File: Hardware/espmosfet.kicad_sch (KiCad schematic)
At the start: 48 parts, among them J1 USB_B_Micro, J2 Conn_01x04_Male, J3 USB_A, J4 Conn_01x04_Male, J5 Conn_01x02_Male, J6 Conn_01x02_Male, J7 Conn_01x03_Male, Q1 AO3400A, Q2 AO3400A, U1 TPS2514A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

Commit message: fix
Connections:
- net +5V: now also U1.5 (IN)
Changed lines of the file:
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@@
+    (stroke (width 0) (type default) (color 0 0 0 0))
+  )
+  (wire (pts (xy 246.38 41.91) (xy 250.19 41.91))
     (stroke (width 0) (type default) (color 0 0 0 0))
   )
@@
     (stroke (width 0) (type default) (color 0 0 0 0))
   )
-  (wire (pts (xy 246.38 41.91) (xy 265.43 41.91))
-    (stroke (width 0) (type default) (color 0 0 0 0))
-  )
   (wire (pts (xy 199.39 144.78) (xy 199.39 147.32))
     (stroke (width 0) (type default) (color 0 0 0 0))
@@
     (stroke (width 0) (type default) (color 0 0 0 0))
   )
-  (wire (pts (xy 250.19 33.02) (xy 250.19 31.75))
-    (stroke (width 0) (type default) (color 0 0 0 0))
-  )
   (wire (pts (xy 116.84 30.48) (xy 110.49 30.48))
     (stroke (width 0) (type default) (color 0 0 0 0))
@@
   )
   (wire (pts (xy 176.53 68.58) (xy 184.15 68.58))
-    (stroke (width 0) (type default) (color 0 0 0 0))
-  )
-  (wire (pts (xy 265.43 41.91) (xy 265.43 26.67))
     (stroke (width 0) (type default) (color 0 0 0 0))
   )
@@
     (pin "5")
   )
-  (symbol (lib_id "power:GND") (at 250.19 33.02 0) (unit 1)
-    (in_bom yes) (on_board yes)
-    (property "Reference" "#PWR03" (id 0) (at 250.19 39.37 0)
-      (effects (font (size 1.27 1.27)) hide)
-    )
-    (property "Value" "GND" (id 1) (at 250.317 37.4142 0))
-    (property "Footprint" "" (id 2) (at 250.19 33.02 0)
-      (effects (font (size 1.27 1.27)) hide)
-    )
-    (property "Datasheet" "" (id 3) (at 250.19 33.02 0)
+  (symbol (lib_id "power:GND") (at 250.19 31.75 90) (unit 1)
+    (in_bom yes) (on_board yes)
+    (property "Reference" "#PWR03" (id 0) (at 256.54 31.75 0)
+      (effects (font (size 1.27 1.27)) hide)
+    )
+    (property "Value" "GND" (id 1) (at 254.5842 31.623 0))
+    (property "Footprint" "" (id 2) (at 250.19 31.75 0)
+      (effects (font (size 1.27 1.27)) hide)
+    )
+    (property "Datasheet" "" (id 3) (at 250.19 31.75 0)
       (effects (font (size 1.27 1.27)) hide)
     )
@@
     )
     (property "Datasheet" "" (id 3) (at 60.96 110.49 0)
+      (effects (font (size 1.27 1.27)) hide)
+    )
+    (pin "1")
+  )
+  (symbol (lib_id "power:+5V") (at 250.19 41.91 270) (unit 1)
+    (in_bom yes) (on_board yes)
+    (property "Reference" "#PWR0124" (id 0) (at 246.38 41.91 0)
+      (effects (font (size 1.27 1.27)) hide)
+    )
+    (property "Value" "+5V" (id 1) (at 254.5842 42.291 0))
+    (property "Footprint" "" (id 2) (at 250.19 41.91 0)
+      (effects (font (size 1.27 1.27)) hide)
+    )
+    (property "Datasheet" "" (id 3) (at 250.19 41.91 0)
       (effects (font (size 1.27 1.27)) hide)
     )
@@
       (reference "#PWR0123") (unit 1) (value "+5V") (footprint "")
     )
+    (path "/0932daf5-053b-464b-bc20-4d6ccf3ec231"
+      (reference "#PWR0124") (unit 1) (value "+5V") (footprint "")
+    )
     (path "/00000000-0000-0000-0000-000061bdbf9c"

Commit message: add USB-C input
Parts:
- added P1: USB_C_Receptacle_USB2.0, Connector_USB:USB_C_Receptacle_XKB_U262-16XN-4BVC11, symbol Connector:USB_C_Receptacle_USB2.0
- added R18: 1M, Resistor_SMD:R_0805_2012Metric, symbol Device:R
- added R19, R20: 5.11k, Resistor_SMD:R_0805_2012Metric, symbol Device:R
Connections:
- net +5VD: now also P1.A4 (VBUS), P1.A9 (VBUS), P1.B4 (VBUS), P1.B9 (VBUS)
- net GND: now also P1.A1 (GND), P1.A12 (GND), P1.B1 (GND), P1.B12 (GND), R18.1, R19.2, R20.2
- new net: P1.A5 (CC1), R20.1
- new net: P1.A6 (D+), P1.B6 (D+)
- new net: P1.A7 (D-), P1.B7 (D-)
- new net: P1.B5 (CC2), R19.1
- new net: P1.S1 (SHIELD), R18.2

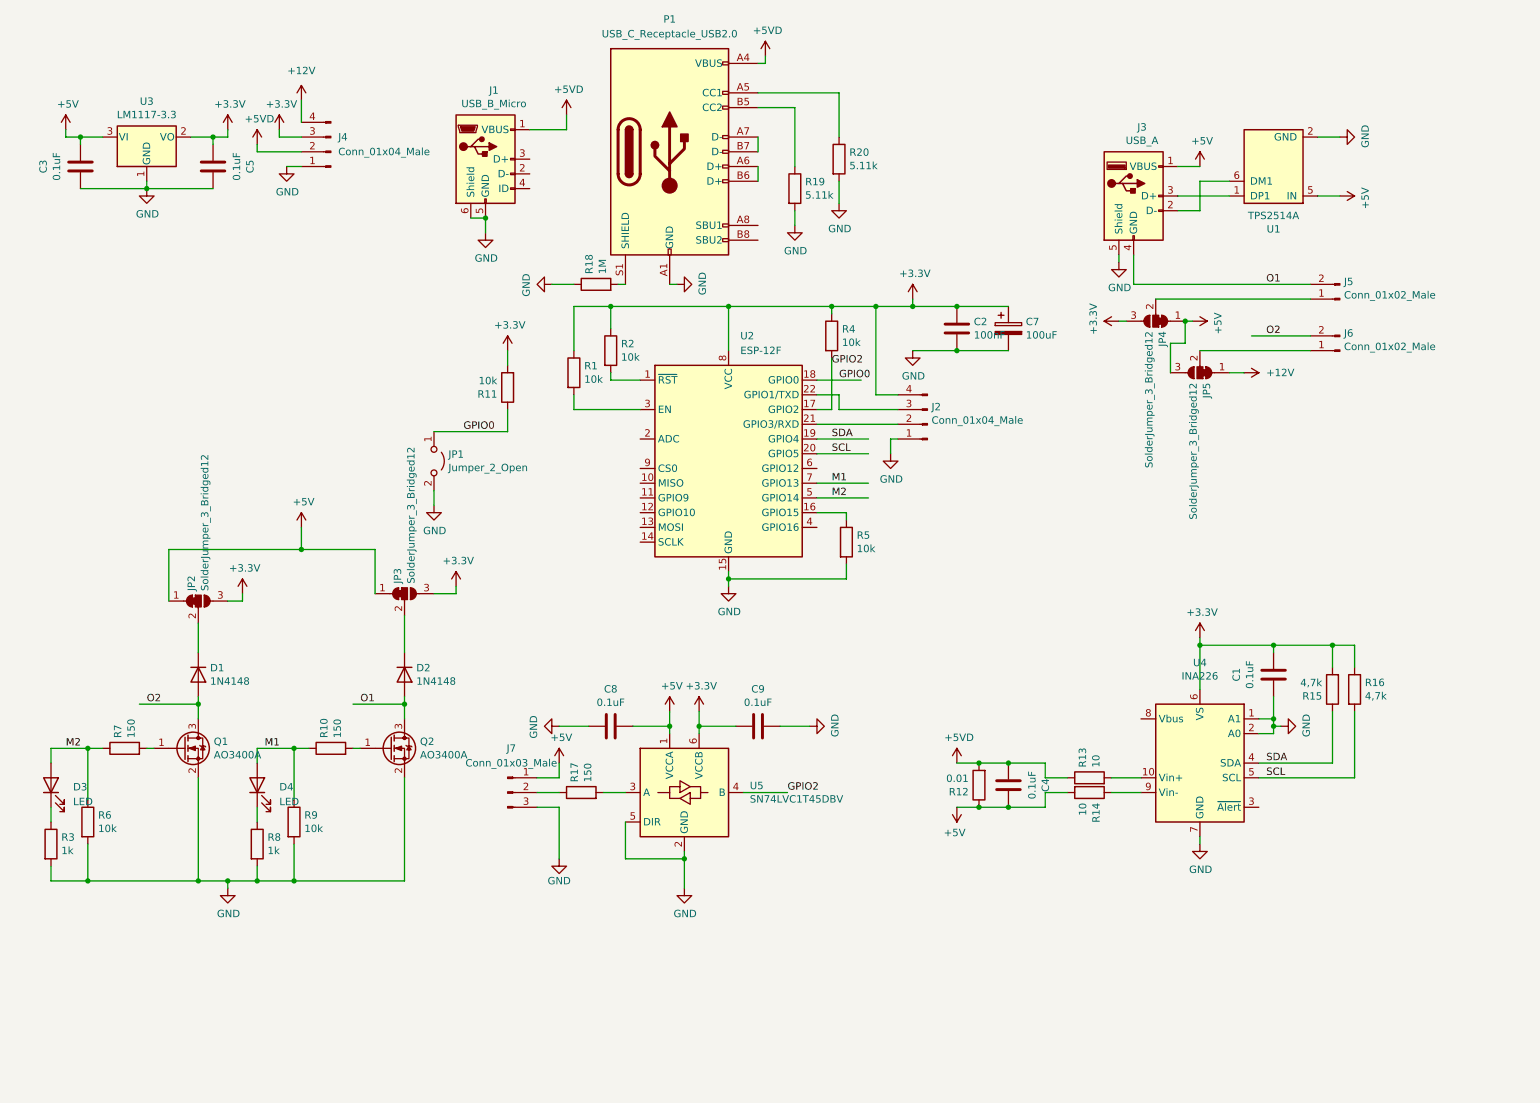
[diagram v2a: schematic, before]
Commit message: add ws2812b on board, add USB-C Output
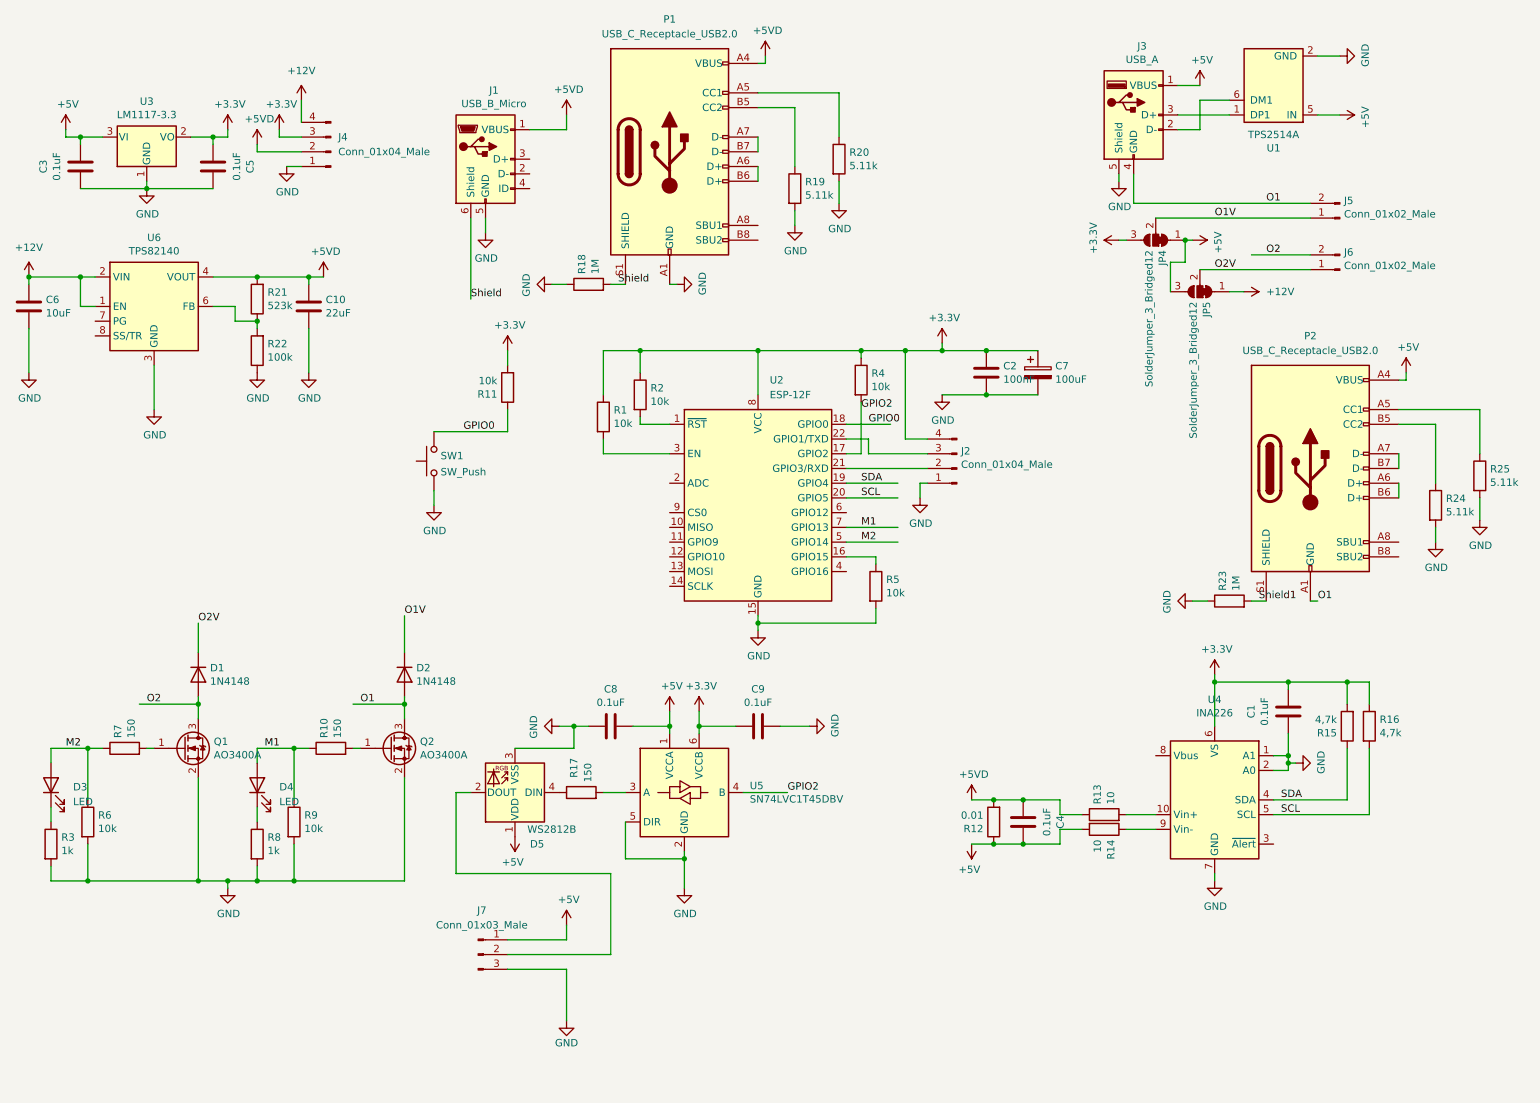
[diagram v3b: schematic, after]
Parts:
- removed JP1: Jumper_2_Open, Jumper:SolderJumper-2_P1.3mm_Open_Pad1.0x1.5mm, symbol Jumper:Jumper_2_Open
- removed JP2, JP3: SolderJumper_3_Bridged12, Jumper:SolderJumper-3_P1.3mm_Bridged12_Pad1.0x1.5mm, symbol Jumper:SolderJumper_3_Bridged12
- added C10: 22uF, Capacitor_SMD:C_1206_3216Metric, symbol Device:C
- added C6: 10uF, Capacitor_SMD:C_0603_1608Metric, symbol Device:C
- added D5: WS2812B, LED_SMD:LED_WS2812B_PLCC4_5.0x5.0mm_P3.2mm, symbol LED:WS2812B
- added P2: USB_C_Receptacle_USB2.0, Connector_USB:USB_C_Receptacle_XKB_U262-16XN-4BVC11, symbol Connector:USB_C_Receptacle_USB2.0
- added R21: 523k, Resistor_SMD:R_0805_2012Metric, symbol Device:R
- added R22: 100k, Resistor_SMD:R_0805_2012Metric, symbol Device:R
- added R23: 1M, Resistor_SMD:R_0805_2012Metric, symbol Device:R
- added R24, R25: 5.11k, Resistor_SMD:R_0805_2012Metric, symbol Device:R
- added SW1: SW_Push, Button_Switch_SMD:SW_Push_SPST_NO_Alps_SKRK, symbol Switch:SW_Push
- added U6: TPS82140, Package_LGA:Texas_SIL0008D_MicroSiP-8-1EP_2.8x3mm_P0.65mm_EP1.1x1.9mm_ThermalVias, symbol Regulator_Switching:TPS82140
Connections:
- net +12V: now also C6.1, U6.1 (EN), U6.2 (VIN)
- net +5V: now also D5.1 (VDD), P2.A4 (VBUS), P2.A9 (VBUS), P2.B4 (VBUS), P2.B9 (VBUS)
- net +5VD: now also C10.1, R21.2, U6.4 (VOUT), U6.5 (VOUT)
- net GND: now also C10.2, C6.2, D5.3 (VSS), R22.1, R23.1, R24.2, R25.2, SW1.1, U6.3 (GND), U6.9 (GND); no longer J1.6 (Shield)
- net GPIO0: now also SW1.2
- net O1: now also P2.A1 (GND), P2.A12 (GND), P2.B1 (GND), P2.B12 (GND)
- net O1V: now reaches D2.1 (K)
- net O1V: now also J5.1 (Pin_1), JP4.2 (C)
- net O2V: now reaches D1.1 (K)
- net O2V: now also J6.1 (Pin_1), JP5.2 (C)
- net at J7.2 (Pin_2): now also D5.2 (DOUT); no longer R17.1
- net Shield: now reaches P1.S1 (SHIELD), R18.2
- net Shield: now also J1.6 (Shield)
- new net: D5.4 (DIN), R17.1
- new net: P2.B5 (CC2), R24.1
- new net: R21.1, R22.2, U6.6 (FB)
- new net: P2.A5 (CC1), R25.1
- new net: P2.A6 (D+), P2.B6 (D+)
- new net: P2.A7 (D-), P2.B7 (D-)
- new net Shield1: P2.S1 (SHIELD), R23.2
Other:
- moved on the sheet: C1, C2, C4, C7, J2, J3, J5, J6, J7, JP4, JP5, R1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

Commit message: update to V2 Version
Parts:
- removed R21: 523k, Resistor_SMD:R_0805_2012Metric, symbol Device:R
- removed R22: 100k, Resistor_SMD:R_0805_2012Metric, symbol Device:R
- removed U6: TPS82140, Package_LGA:Texas_SIL0008D_MicroSiP-8-1EP_2.8x3mm_P0.65mm_EP1.1x1.9mm_ThermalVias, symbol Regulator_Switching:TPS82140
- added U6: LMZM23601V5, Package_LGA:Texas_SIL0010A_MicroSiP-10-1EP_3.8x3mm_P0.6mm_EP0.7x2.9mm_ThermalVias, symbol Regulator_Switching:LMZM23601V5
- C10: footprint Capacitor_SMD:C_1206_3216Metric -> Capacitor_SMD:C_0805_2012Metric
- R19, R20, R24, R25: footprint Resistor_SMD:R_0805_2012Metric -> Resistor_SMD:R_0603_1608Metric
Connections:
- net +12V: now also U6.3 (VIN), U6.4 (EN)
- net +5VD: now also U6.6 (VOUT), U6.7 (FB)
- net GND: now also U6.1 (GND), U6.11 (GND), U6.2 (MODE/SYNC)
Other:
- moved on the sheet: C10, C6

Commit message: adjust Readme
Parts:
- added JP1: Jumper_2_Open, Jumper:SolderJumper-2_P1.3mm_Open_Pad1.0x1.5mm, symbol Jumper:Jumper_2_Open
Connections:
- net at D5.2 (DOUT), J7.2 (Pin_2): now also JP1.1 (A)
- net at D5.4 (DIN), R17.1: now also JP1.2 (B)
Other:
- moved on the sheet: R17
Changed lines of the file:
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@@
   (junction (at 31.75 73.66) (diameter 0) (color 0 0 0 0)
   )
+  (junction (at 124.46 158.75) (diameter 0) (color 0 0 0 0)
+  )
   (junction (at 195.58 146.05) (diameter 0) (color 0 0 0 0)
   )
@@
   (junction (at 27.94 88.9) (diameter 0) (color 0 0 0 0)
   )
+  (junction (at 115.57 144.78) (diameter 0) (color 0 0 0 0)
+  )
   (junction (at 181.61 68.58) (diameter 0) (color 0 0 0 0)
   )
@@
     (stroke (width 0) (type default) (color 0 0 0 0))
   )
+  (wire (pts (xy 115.57 148.59) (xy 115.57 144.78))
+    (stroke (width 0) (type default) (color 0 0 0 0))
+  )
   (wire (pts (xy 44.45 40.64) (xy 55.88 40.64))
     (stroke (width 0) (type default) (color 0 0 0 0))
@@
     (stroke (width 0) (type default) (color 0 0 0 0))
   )
-  (wire (pts (xy 123.19 144.78) (xy 127 144.78))
-    (stroke (width 0) (type default) (color 0 0 0 0))
-  )
   (wire (pts (xy 27.94 157.48) (xy 27.94 160.02))
     (stroke (width 0) (type default) (color 0 0 0 0))
@@
     (stroke (width 0) (type default) (color 0 0 0 0))
   )
+  (wire (pts (xy 124.46 144.78) (xy 127 144.78))
+    (stroke (width 0) (type default) (color 0 0 0 0))
+  )
   (wire (pts (xy 88.9 132.08) (xy 88.9 129.54))
     (stroke (width 0) (type default) (color 0 0 0 0))
@@
     (stroke (width 0) (type default) (color 0 0 0 0))
   )
+  (wire (pts (xy 115.57 144.78) (xy 116.84 144.78))
+    (stroke (width 0) (type default) (color 0 0 0 0))
+  )
   (wire (pts (xy 63.5 160.02) (xy 69.85 160.02))
     (stroke (width 0) (type default) (color 0 0 0 0))
@@
   )
   (wire (pts (xy 118.11 137.16) (xy 118.11 133.35))
+    (stroke (width 0) (type default) (color 0 0 0 0))
+  )
+  (wire (pts (xy 124.46 148.59) (xy 115.57 148.59))
     (stroke (width 0) (type default) (color 0 0 0 0))
   )
@@
     )
     (property "Datasheet" "~" (id 3) (at 88.9 87.63 0)
+      (effects (font (size 1.27 1.27)) hide)
+    )
+    (pin "1")
+    (pin "2")
+  )
+  (symbol (lib_id "Jumper:Jumper_2_Open") (at 124.46 153.67 90) (unit 1)
+    (in_bom yes) (on_board yes)
+    (property "Reference" "JP1" (id 0) (at 120.65 151.13 90)
+      (effects (font (size 1.27 1.27)) (justify right))
+    )
+    (property "Value" "Jumper_2_Open" (id 1) (at 113.03 157.48 90)
+      (effects (font (size 1.27 1.27)) (justify right))
+    )
+    (property "Footprint" "Jumper:SolderJumper-2_P1.3mm_Open_Pad1.0x1.5mm" (id 2) (at 124.46 153.67 0)
+      (effects (font (size 1.27 1.27)) hide)
+    )
+    (property "Datasheet" "~" (id 3) (at 124.46 153.67 0)
       (effects (font (size 1.27 1.27)) hide)
     )
@@
     (pin "2")
   )
-  (symbol (lib_id "Device:R") (at 119.38 144.78 90) (unit 1)
-    (in_bom yes) (on_board yes)
-    (property "Reference" "R17" (id 0) (at 118.11 142.24 0)
-      (effects (font (size 1.27 1.27)) (justify left))
-    )
-    (property "Value" "150" (id 1) (at 120.523 143.002 0)
-      (effects (font (size 1.27 1.27)) (justify left))
-    )
-    (property "Footprint" "Resistor_SMD:R_0805_2012Metric" (id 2) (at 119.38 146.558 90)
-      (effects (font (size 1.27 1.27)) hide)
-    )
-    (property "Datasheet" "~" (id 3) (at 119.38 144.78 0)
+  (symbol (lib_id "Device:R") (at 120.65 144.78 90) (unit 1)
+    (in_bom yes) (on_board yes)
+    (property "Reference" "R17" (id 0) (at 119.38 142.24 0)
+      (effects (font (size 1.27 1.27)) (justify left))
+    )
+    (property "Value" "150" (id 1) (at 121.793 143.002 0)
+      (effects (font (size 1.27 1.27)) (justify left))
+    )
+    (property "Footprint" "Resistor_SMD:R_0805_2012Metric" (id 2) (at 120.65 146.558 90)
+      (effects (font (size 1.27 1.27)) hide)
+    )
+    (property "Datasheet" "~" (id 3) (at 120.65 144.78 0)
       (effects (font (size 1.27 1.27)) hide)
     )
@@
       (reference "J7") (unit 1) (value "Conn_01x03_Male") (footprint "Connector_PinHeader_2.54mm:PinHeader_1x03_P2.54mm_Vertical")
     )
+    (path "/57e87282-fda0-4fe1-9c9f-ad677bd23537"
+      (reference "JP1") (unit 1) (value "Jumper_2_Open") (footprint "Jumper:SolderJumper-2_P1.3mm_Open_Pad1.0x1.5mm")
+    )
     (path "/66501696-d13c-4e27-b64d-57712750e262"
